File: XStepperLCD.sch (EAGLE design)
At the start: 31 parts, among them Q2 16 MHZ, U1 LCD-16X2NOHOLES

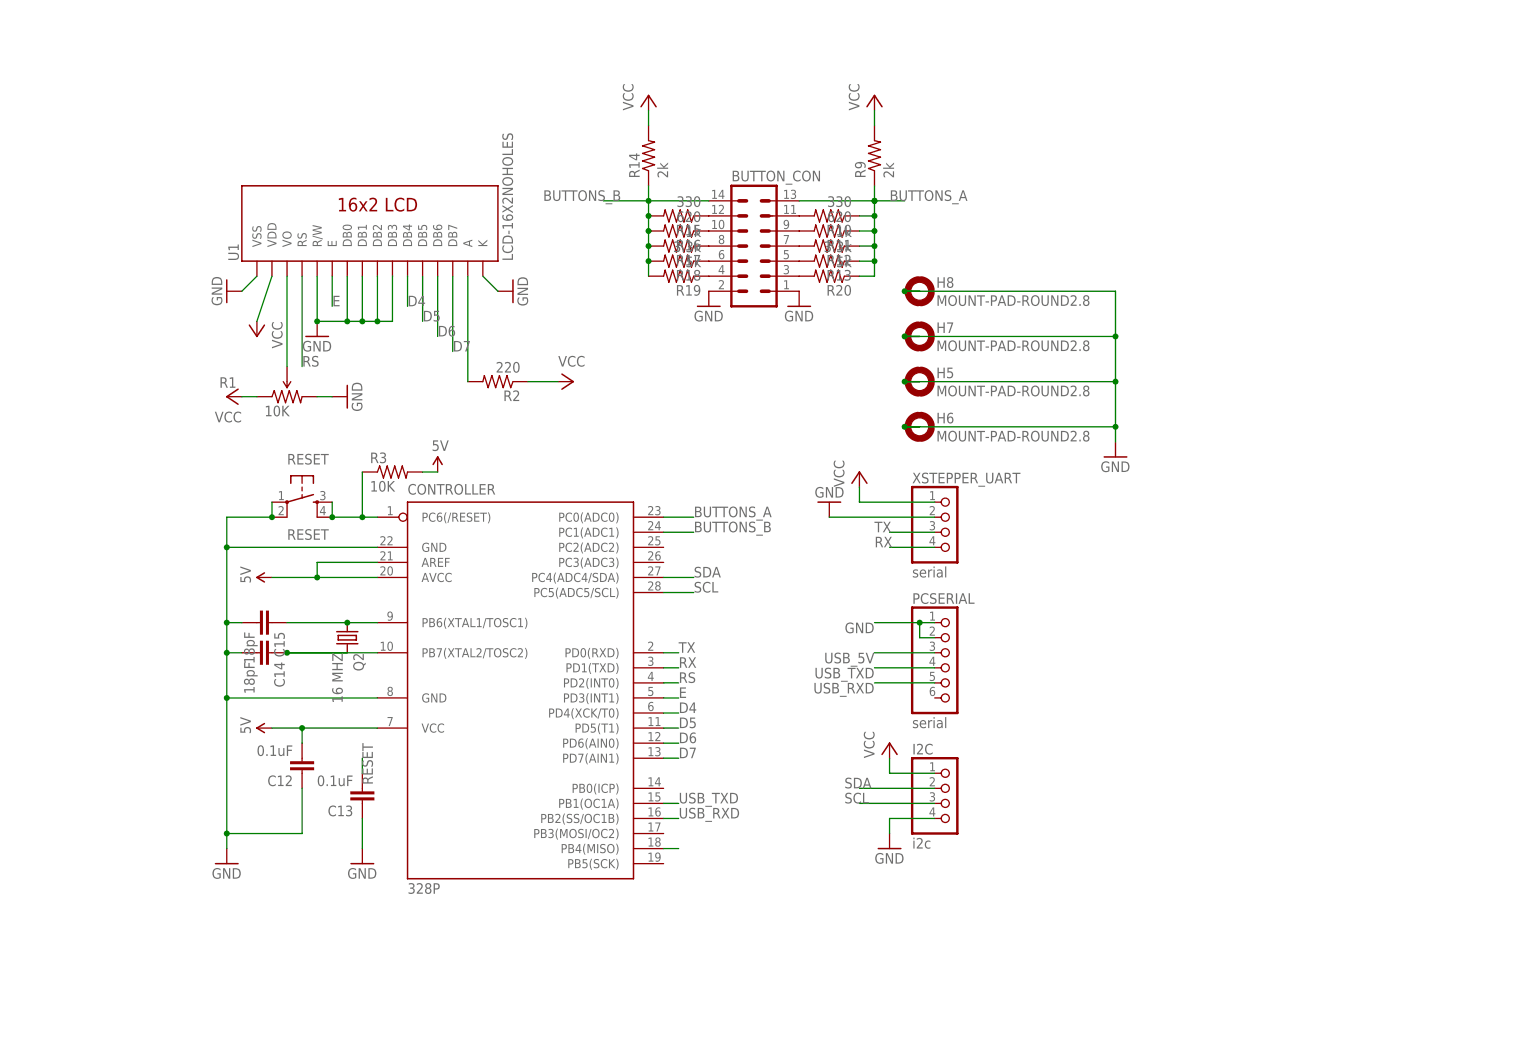
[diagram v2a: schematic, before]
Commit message: pov, duo led, sketchup
- add duo led
- add icsp header
- create povray file
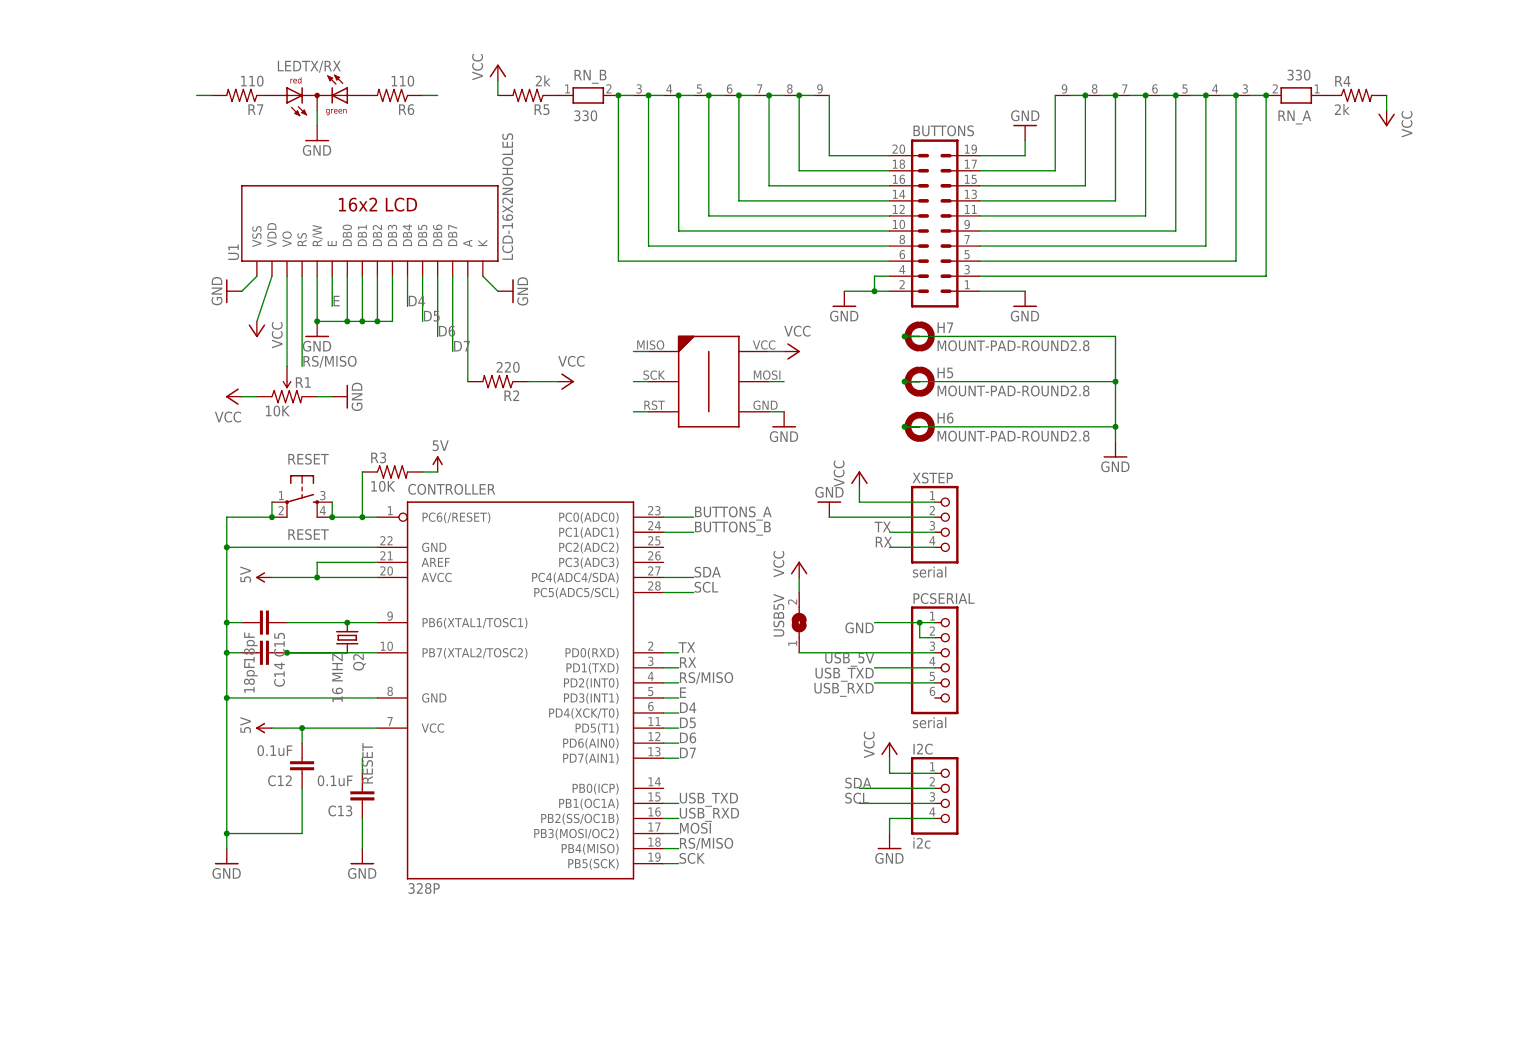
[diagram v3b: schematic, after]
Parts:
- removed BUTTON_CON: (no value), con-ml:ML14
- removed H8: MOUNT-PAD-ROUND2.8, holes:MOUNT-PAD-ROUND2.8
- removed R10, R15: 330, SparkFun-Resistors:RESISTORAXIAL-0.3
- removed R11, R16: 620, SparkFun-Resistors:RESISTORAXIAL-0.3
- removed R12, R17: 1k, SparkFun-Resistors:RESISTORAXIAL-0.3
- removed R13, R18: 3.3k, SparkFun-Resistors:RESISTORAXIAL-0.3
- removed R14, R9: 2k, SparkFun-Resistors:RESISTORAXIAL-0.3
- removed R19, R20: 5k, SparkFun-Resistors:RESISTORAXIAL-0.3
- added BUTTONS: (no value), con-ml:ML20
- added ICSP: ICSP, avr-7:AVR-ISP-6-EDGE
- added LEDTX/RX: (no value), led:DUOLED2X5
- added R4, R5: 2k, SparkFun-Resistors:RESISTORAXIAL-0.3
- added R6, R7: 110, SparkFun-Resistors:RESISTORAXIAL-0.3
- added RN_A, RN_B: 330, resistor-net:RN08
- added USB5V: (no value), jumper:SJ
- R1: device SparkFun-Electromechanical:TRIMPOT-PTH-KNOB -> SparkFun-Electromechanical:TRIMPOT3362U-2
- R2: device SparkFun-Resistors:RESISTORAXIAL-0.3 -> SparkFun-Resistors:RESISTORPTH-1/6W
- renumbered XSTEPPER_UART to XSTEP
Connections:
- removed net RS: 328P.PD2(INT0), U1.RS
- new net MOSI: 328P.PB3(MOSI/OC2), ICSP.P$5
- new net N$10: BUTTONS.5, RN_A.3
- new net N$17: BUTTONS.9, RN_A.5
- new net N$18: BUTTONS.11, RN_A.6
- new net N$19: BUTTONS.18, RN_B.8
- new net N$20: BUTTONS.20, RN_B.9
- new net N$21: LEDTX/RX.AG, R6.2
- new net N$22: LEDTX/RX.AR, R7.1
- new net N$7: BUTTONS.6, RN_B.2
- new net N$8: BUTTONS.8, RN_B.3
- new net N$9: BUTTONS.3, RN_A.2
- new net RS/MISO: 328P.PB4(MISO), 328P.PD2(INT0), ICSP.P$1, U1.RS
- new net SCK: 328P.PB5(SCK), ICSP.P$2
- net BUTTONS_A: no longer BUTTON_CON.13, R10.1, R11.1, R12.1, R13.1, R20.1, R9.1
- net BUTTONS_B: no longer BUTTON_CON.14, R14.1, R15.2, R16.2, R17.2, R18.2, R19.2
- net D4: now also 328P.PD4(XCK/T0)
- net GND: now also BUTTONS.1, BUTTONS.19, BUTTONS.2, BUTTONS.4, ICSP.P$4, LEDTX/RX.C; no longer BUTTON_CON.1, BUTTON_CON.2, H8.MOUNT
- net N$11: now also BUTTONS.10, RN_B.4; no longer BUTTON_CON.12, R15.1
- net N$12: now also BUTTONS.12, RN_B.5; no longer BUTTON_CON.10, R16.1
- net N$13: now also BUTTONS.14, RN_B.6; no longer BUTTON_CON.8, R17.1
- net N$14: now also R5.1, RN_B.1; no longer BUTTON_CON.6, R18.1
- net N$15: now also BUTTONS.16, RN_B.7; no longer BUTTON_CON.4, R19.1
- net N$16: now also BUTTONS.7, RN_A.4; no longer BUTTON_CON.3, R20.2
- net N$3: now also R4.1, RN_A.1; no longer BUTTON_CON.11, R10.2
- net N$4: now also BUTTONS.13, RN_A.7; no longer BUTTON_CON.9, R11.2
- net N$5: now also BUTTONS.15, RN_A.8; no longer BUTTON_CON.7, R12.2
- net N$6: now also BUTTONS.17, RN_A.9; no longer BUTTON_CON.5, R13.2
- net RESET: now also ICSP.P$3
- net RX: now also R6.1
- net TX: now also R7.2
- net USB_5V: now also USB5V.1
- net VCC: now also ICSP.P$6, R4.2, R5.2, USB5V.2; no longer R14.2, R9.2

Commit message: - add 2 connects for potentiometers
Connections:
- removed net 5V: 328P.AREF, 328P.AVCC, 328P.VCC@1, C12.2, R3.2
- new net POT_A: 328P.PC2(ADC2), BUTTONS.4
- new net POT_B: 328P.PC3(ADC3), BUTTONS.2
- net GND: no longer BUTTONS.2, BUTTONS.4
- net VCC: now also 328P.AREF, 328P.AVCC, 328P.VCC@1, C12.2, R3.2

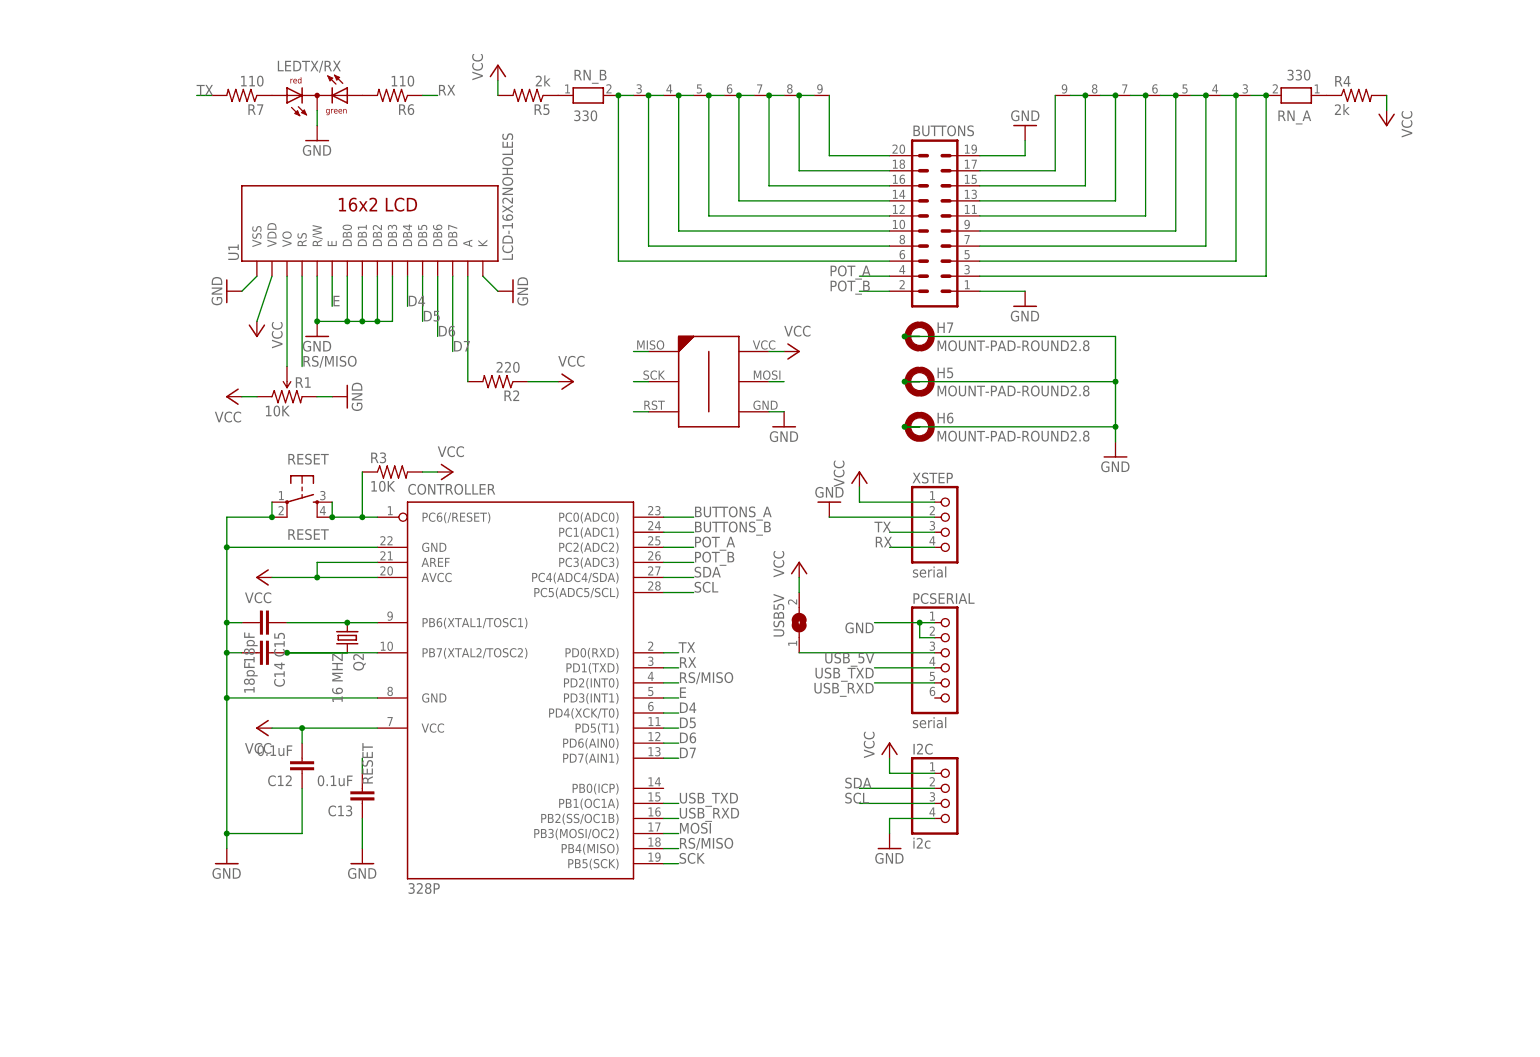
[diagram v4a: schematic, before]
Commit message: - published to ITEAD order number 100015612
- official Version XLCD 0.1
- add some text
- 3 pin header
- changes from Matt
- GND Polygon fix
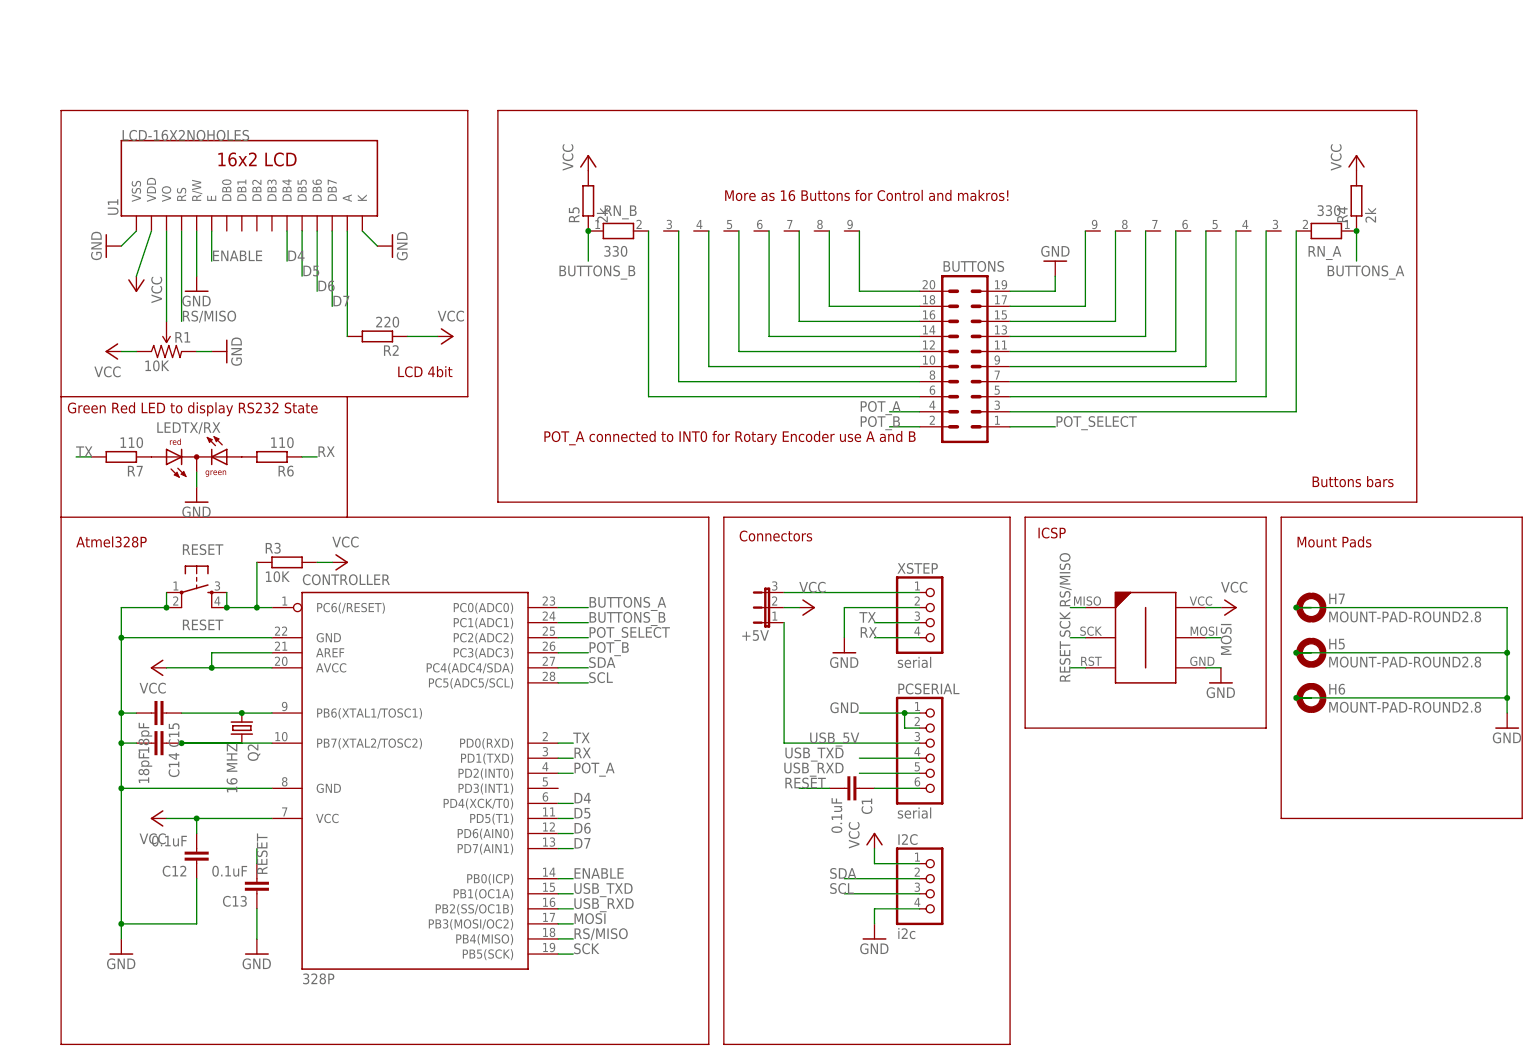
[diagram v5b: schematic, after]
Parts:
- removed USB5V: (no value), jumper:SJ
- added +5V: (no value), jumper:JP2E
- added C1: 0.1uF, resistor:C-EU025-025X050
- R2: device SparkFun-Resistors:RESISTORPTH-1/6W -> resistor:R-EU_0204/7
- R3, R4, R5, R6, R7: device SparkFun-Resistors:RESISTORAXIAL-0.3 -> resistor:R-EU_0204/7
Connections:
- removed net E: 328P.PD3(INT1), U1.E
- removed net N$3: R4.1, RN_A.1
- new net ENABLE: 328P.PB0(ICP), U1.E
- new net POT_SELECT: 328P.PC2(ADC2), BUTTONS.1
- new net XSTEP_5V: +5V.3, XSTEP.1
- net BUTTONS_A: now also R4.1, RN_A.1
- net BUTTONS_B: now also R5.1, RN_B.1
- net GND: no longer BUTTONS.1, U1.DB0, U1.DB1, U1.DB2, U1.DB3
- net N$14: now also C1.1, PCSERIAL.6; no longer R5.1, RN_B.1
- net POT_A: now also 328P.PD2(INT0); no longer 328P.PC2(ADC2)
- net RESET: now also C1.2
- net RS/MISO: no longer 328P.PD2(INT0)
- net USB_5V: now also +5V.1; no longer USB5V.1
- net VCC: now also +5V.2; no longer USB5V.2, XSTEP.1
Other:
- note added: "Atmel328P"
- note added: "Buttons bars"
- note added: "Connectors"
- note added: "Green Red LED to display RS232 State"
- note added: "ICSP"
- note added: "LCD 4bit"
- note added: "More as 16 Buttons for Control and makros!"
- note added: "Mount Pads"
- note added: "POT_A connected to INT0 for Rotary Encoder use A and B"
- moved on the sheet: 328P, BUTTONS, C12, C13, C14, C15, H5, H6, H7, I2C, LEDTX/RX, PCSERIAL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
